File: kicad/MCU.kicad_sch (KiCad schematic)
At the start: 75 parts

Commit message: Fixed symbol missmatches from upgrading to kicad 6
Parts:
- NT? (x4): symbol Device:Net-Tie_2 -> Device:NetTie_2
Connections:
- net +3V3: now also NT?.2, NT?.2, NT?.2, NT?.2
- net VDD1: now also NT?.1
- net VDDA: now also NT?.1
- net VDDSD: now also NT?.1
- net VREFSD: now also NT?.1

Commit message: Fixed broken connections
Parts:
- removed NT? (x4): Net-Tie_2, symbol Device:NetTie_2
- SW1, SW2: renamed from SW?; symbol Device:Rotary_Encoder_Switch -> Device:RotaryEncoder_Switch
- gave numbers to parts that had none: 69
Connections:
- net VDD1 is gone; now on net +3V3: C59.1, C63.1, C69.1, C70.1, C71.1, U8.17 (VDD), U8.48 (VDD)
- net VDDA is gone; now on net +3V3: C56.2, C60.2, C66.2, U8.9 (VDDA)
- net VDDSD is gone; now on net +3V3: C57.2, C61.2, C67.2, U8.24 (VDDSD)
- net VREFSD is gone; now on net +3V3: C58.2, C62.2, C68.2, U8.25 (VREFSD+)
- net GND: now also SW1.C, SW1.S2, SW2.S2
- net GNDREF: now also SW2.C
- net at R78.2: now also SW2.S1
- net at R73.1, R76.1: now also SW2.A
- net at R74.2, R77.1: now also SW2.B
- net at R62.2, R64.1: now also SW1.B
- net at R61.1, R63.1: now also SW1.A
- net at R67.2: now also SW1.S1
- no-connect marks 6 -> 7
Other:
- moved on the sheet: C59, C63, C69, C70, C71

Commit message: Yeeted SMPSs and small changes
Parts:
- removed C70: 100nF, Capacitor_SMD:C_0805_2012Metric_Pad1.15x1.40mm_HandSolder, symbol Device:C_Small
- added NT? (x4): NetTie_2, symbol Device:NetTie_2
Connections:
- net +3V3: now also NT?.2, NT?.2, NT?.2, NT?.2; no longer C56.2, C57.2, C58.2, C59.1, C60.2, C61.2, C62.2, C63.1, C66.2, C67.2, C68.2, C69.1, C71.1, SW3.2, U8.17 (VDD), U8.24 (VDDSD), U8.25 (VREFSD+), U8.48 (VDD), U8.9 (VDDA)
- net SVOUT_RANGE: no longer names the net of U8.20 (PB2)
- new net VDD1: C59.1, C63.1, C69.1, C71.1, NT?.1, SW3.2, U8.17 (VDD), U8.48 (VDD)
- new net VDDA: C56.2, C60.2, C66.2, NT?.1, U8.9 (VDDA)
- new net VDDSD: C57.2, C61.2, C67.2, NT?.1, U8.24 (VDDSD)
- new net VREFSD: C58.2, C62.2, C68.2, NT?.1, U8.25 (VREFSD+)
- no-connect marks 7 -> 8
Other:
- moved on the sheet: C71

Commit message: Added option to power the 1K5 pullup from 3V3 or VBUS
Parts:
- added JP?: Jumper_2_Open, symbol Jumper:Jumper_2_Open
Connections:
- net +3V3: now also JP?.2 (B)
- net at C73.2, R69.2, R70.2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: now also JP?.1 (A)
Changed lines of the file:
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@@
+    (stroke (width 0) (type default) (color 0 0 0 0))
+  )
+  (wire (pts (xy 85.598 99.06) (xy 82.042 99.06))
     (stroke (width 0) (type default) (color 0 0 0 0))
   )
@@
     (stroke (width 0.254) (type default) (color 0 0 0 0))
   )
+  (wire (pts (xy 82.042 99.06) (xy 82.042 101.346))
+    (stroke (width 0) (type default) (color 0 0 0 0))
+  )
   (wire (pts (xy 31.75 188.722) (xy 31.75 189.992))
     (stroke (width 0) (type default) (color 0 0 0 0))
@@
     (stroke (width 0) (type default) (color 0 0 0 0))
   )
+  (wire (pts (xy 102.616 98.044) (xy 102.616 99.06))
+    (stroke (width 0) (type default) (color 0 0 0 0))
+  )
   (polyline (pts (xy 75.565 79.375) (xy 75.565 15.24))
     (stroke (width 0.254) (type default) (color 0 0 0 0))
@@
     (stroke (width 0) (type default) (color 0 0 0 0))
   )
+  (wire (pts (xy 80.01 101.346) (xy 80.01 103.632))
+    (stroke (width 0) (type default) (color 0 0 0 0))
+  )
   (wire (pts (xy 87.63 106.172) (xy 90.17 106.172))
     (stroke (width 0) (type default) (color 0 0 0 0))
@@
   )
   (wire (pts (xy 153.162 184.15) (xy 162.052 184.15))
+    (stroke (width 0) (type default) (color 0 0 0 0))
+  )
+  (wire (pts (xy 82.042 101.346) (xy 80.01 101.346))
+    (stroke (width 0) (type default) (color 0 0 0 0))
+  )
+  (wire (pts (xy 102.616 99.06) (xy 95.758 99.06))
     (stroke (width 0) (type default) (color 0 0 0 0))
   )
@@
     (pin "3")
   )
+  (symbol (lib_id "Jumper:Jumper_2_Open") (at 90.678 99.06 0) (unit 1)
+    (in_bom yes) (on_board yes) (fields_autoplaced)
+    (property "Reference" "JP?" (id 0) (at 90.678 92.71 0))
+    (property "Value" "Jumper_2_Open" (id 1) (at 90.678 95.25 0))
+    (property "Footprint" "" (id 2) (at 90.678 99.06 0)
+      (effects (font (size 1.27 1.27)) hide)
+    )
+    (property "Datasheet" "~" (id 3) (at 90.678 99.06 0)
+      (effects (font (size 1.27 1.27)) hide)
+    )
+    (pin "1")
+    (pin "2")
+  )
   (symbol (lib_id "Device:NetTie_2") (at 61.214 68.834 0) (unit 1)
     (in_bom yes) (on_board yes) (fields_autoplaced)
@@
     (pin "2")
   )
+  (symbol (lib_id "power:+3V3") (at 102.616 98.044 0) (unit 1)
+    (in_bom yes) (on_board yes) (fields_autoplaced)
+    (property "Reference" "#PWR?" (id 0) (at 102.616 101.854 0)
+      (effects (font (size 1.27 1.27)) hide)
+    )
+    (property "Value" "+3V3" (id 1) (at 102.616 92.964 0))
+    (property "Footprint" "" (id 2) (at 102.616 98.044 0)
+      (effects (font (size 1.27 1.27)) hide)
+    )
+    (property "Datasheet" "" (id 3) (at 102.616 98.044 0)
+      (effects (font (size 1.27 1.27)) hide)
+    )
+    (pin "1")
+  )
   (symbol (lib_id "Device:NetTie_2") (at 51.816 37.592 0) (unit 1)

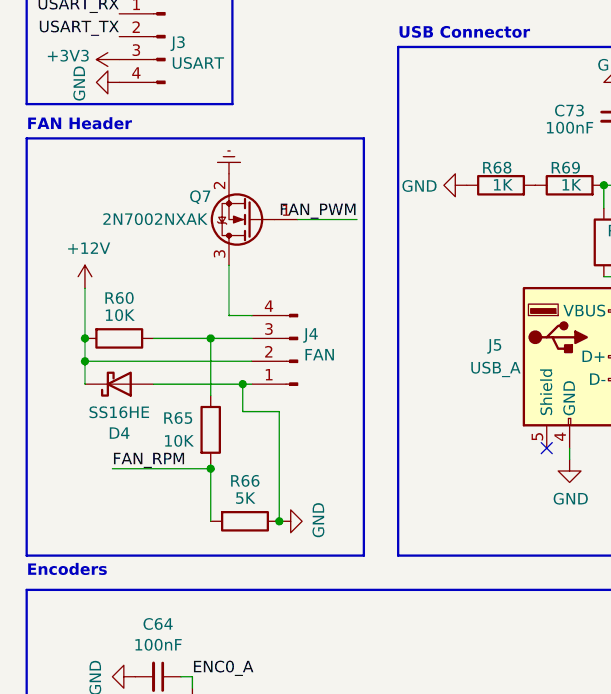
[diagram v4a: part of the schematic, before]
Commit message: Fixed fan rpm reading circuitry
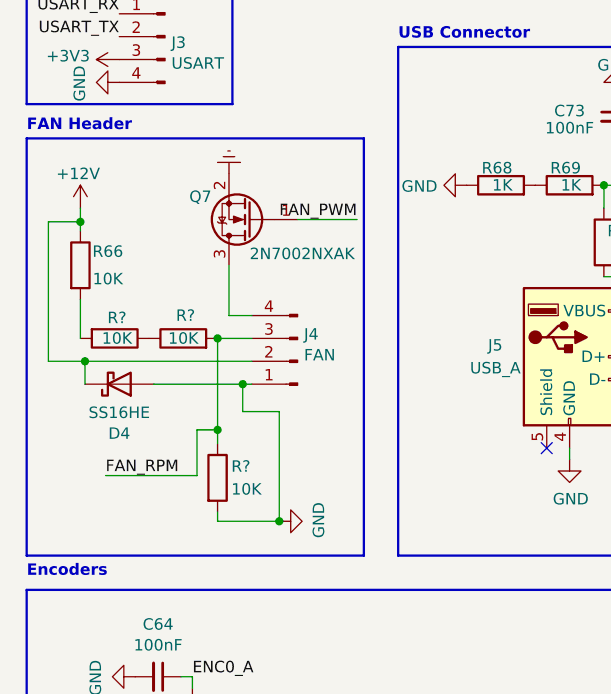
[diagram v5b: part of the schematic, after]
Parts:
- removed R60, R65: 10K, symbol Device:R
- added R? (x3): 10K, symbol Device:R
- R66: value 5K -> 10K
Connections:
- net +12V: now also R66.1
- net FAN_RPM: now also J4.3 (Pin_3), R?.1, R?.2; no longer R66.2
- net GND: now also R?.2; no longer R66.1
- new net: R66.2, R?.2
- new net: R?.1, R?.1
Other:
- moved on the sheet: R66

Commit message: Changes
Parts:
- removed R82: 1K, Resistor_SMD:R_0805_2012Metric_Pad1.15x1.40mm_HandSolder, symbol Device:R
- added R? (x2): 100R, symbol Device:R
- J4: footprint (none) -> Connector:FanPinHeader_1x04_P2.54mm_Vertical
- R81: value 1K -> 4K7
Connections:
- net FAN_PWM: now also R?.2; no longer Q7.1 (G)
- net FAN_RPM: now also R?.1; no longer J4.3 (Pin_3), R?.1, R?.2
- new net: J4.3 (Pin_3), R?.1, R?.2, R?.2
- new net: Q7.1 (G), R?.1
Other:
- moved on the sheet: Q7
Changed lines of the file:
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@@
   (junction (at 36.83 73.914) (diameter 0) (color 0 0 0 0)
   )
-  (junction (at 145.542 184.15) (diameter 0) (color 0 0 0 0)
-  )
   (junction (at 80.01 106.172) (diameter 0) (color 0 0 0 0)
   )
@@
   )
   (junction (at 36.83 54.102) (diameter 0) (color 0 0 0 0)
-  )
-  (junction (at 153.162 184.15) (diameter 0) (color 0 0 0 0)
   )
   (junction (at 31.75 173.482) (diameter 0) (color 0 0 0 0)
@@
     (stroke (width 0) (type default) (color 0 0 0 0))
   )
-  (wire (pts (xy 43.434 109.982) (xy 50.038 109.982))
-    (stroke (width 0) (type default) (color 0 0 0 0))
-  )
   (wire (pts (xy 29.21 178.562) (xy 31.75 178.562))
     (stroke (width 0) (type default) (color 0 0 0 0))
@@
     (stroke (width 0) (type default) (color 0 0 0 0))
   )
+  (wire (pts (xy 35.814 118.364) (xy 35.814 120.65))
+    (stroke (width 0) (type default) (color 0 0 0 0))
+  )
   (polyline (pts (xy 121.92 147.32) (xy 121.92 90.805))
     (stroke (width 0.254) (type default) (color 0 0 0 0))
@@
     (stroke (width 0) (type default) (color 0 0 0 0))
   )
+  (wire (pts (xy 35.814 120.65) (xy 38.354 120.65))
+    (stroke (width 0) (type default) (color 0 0 0 0))
+  )
   (wire (pts (xy 150.622 40.132) (xy 148.844 40.132))
     (stroke (width 0) (type default) (color 0 0 0 0))
@@
     (stroke (width 0) (type default) (color 0 0 0 0))
   )
-  (wire (pts (xy 35.814 115.062) (xy 35.814 120.65))
-    (stroke (width 0) (type default) (color 0 0 0 0))
-  )
   (wire (pts (xy 145.542 124.46) (xy 145.542 126.492))
     (stroke (width 0) (type default) (color 0 0 0 0))
@@
     (stroke (width 0) (type default) (color 0 0 0 0))
   )
-  (wire (pts (xy 153.162 184.15) (xy 153.162 187.96))
-    (stroke (width 0) (type default) (color 0 0 0 0))
-  )
   (polyline (pts (xy 130.81 151.13) (xy 13.335 151.13))
     (stroke (width 0.254) (type default) (color 0 0 0 0))
@@
     (stroke (width 0) (type default) (color 0 0 0 0))
   )
-  (wire (pts (xy 22.098 138.43) (xy 32.258 138.43))
+  (wire (pts (xy 16.002 138.43) (xy 24.638 138.43))
     (stroke (width 0) (type default) (color 0 0 0 0))
   )
@@
     (stroke (width 0) (type default) (color 0 0 0 0))
   )
+  (wire (pts (xy 42.672 109.982) (xy 50.292 109.982))
+    (stroke (width 0) (type default) (color 0 0 0 0))
+  )
   (wire (pts (xy 120.65 45.212) (xy 150.622 45.212))
     (stroke (width 0) (type default) (color 0 0 0 0))
@@
     (stroke (width 0) (type default) (color 0 0 0 0))
   )
+  (wire (pts (xy 27.432 115.062) (xy 27.432 118.364))
+    (stroke (width 0) (type default) (color 0 0 0 0))
+  )
   (wire (pts (xy 36.83 68.834) (xy 48.26 68.834))
     (stroke (width 0) (type default) (color 0 0 0 0))
   )
-  (wire (pts (xy 35.814 120.65) (xy 38.354 120.65))
-    (stroke (width 0) (type default) (color 0 0 0 0))
-  )
   (wire (pts (xy 96.52 113.792) (xy 96.52 116.332))
     (stroke (width 0) (type default) (color 0 0 0 0))
@@
     (stroke (width 0) (type default) (color 0 0 0 0))
   )
+  (wire (pts (xy 27.432 118.364) (xy 35.814 118.364))
+    (stroke (width 0) (type default) (color 0 0 0 0))
+  )
   (polyline (pts (xy 165.735 147.32) (xy 165.735 120.65))
     (stroke (width 0.254) (type default) (color 0 0 0 0))
-  )
-  (wire (pts (xy 145.542 184.15) (xy 145.542 187.96))
-    (stroke (width 0) (type default) (color 0 0 0 0))
   )
   (wire (pts (xy 160.782 186.69) (xy 160.782 188.722))
@@
     (effects (font (size 1.27 1.27)) (justify right bottom))
   )
-  (label "FAN_RPM" (at 22.098 138.43 0)
+  (label "FAN_RPM" (at 16.002 138.43 0)
     (effects (font (size 1.27 1.27)) (justify left bottom))
   )
@@
     (effects (font (size 1.27 1.27)) (justify right bottom))
   )
-  (label "FAN_PWM" (at 50.038 109.982 180)
+  (label "FAN_PWM" (at 50.292 109.982 180)
     (effects (font (size 1.27 1.27)) (justify right bottom))
   )
@@
     (pin "1")
   )
-  (symbol (lib_id "Device:R") (at 149.352 187.96 90) (unit 1)
-    (in_bom yes) (on_board yes)
-    (property "Reference" "R82" (id 0) (at 143.002 186.69 90))
-    (property "Value" "1K" (id 1) (at 154.432 186.69 90))
-    (property "Footprint" "Resistor_SMD:R_0805_2012Metric_Pad1.15x1.40mm_HandSolder" (id 2) (at 149.352 189.738 90)
-      (effects (font (size 1.27 1.27)) hide)
-    )
-    (property "Datasheet" "https://www.mouser.se/datasheet/2/447/PYu-RT_1-to-0.01_RoHS_L_9-1222720.pdf" (id 3) (at 149.352 187.96 0)
-      (effects (font (size 1.27 1.27)) hide)
-    )
-    (property "MPN" "RT0805FRE071KL" (id 4) (at 149.352 187.96 0)
-      (effects (font (size 1.27 1.27)) hide)
-    )
-    (pin "1")
-    (pin "2")
-  )
   (symbol (lib_id "power:+3V3") (at 140.462 184.15 90) (unit 1)
     (in_bom yes) (on_board yes)
@@
   (symbol (lib_id "Device:R") (at 149.352 184.15 90) (unit 1)
     (in_bom yes) (on_board yes)
-    (property "Reference" "R81" (id 0) (at 143.002 182.88 90))
-    (property "Value" "1K" (id 1) (at 154.432 182.88 90))
+    (property "Reference" "R81" (id 0) (at 149.352 186.436 90))
+    (property "Value" "4K7" (id 1) (at 149.352 184.15 90))
     (property "Footprint" "Resistor_SMD:R_0805_2012Metric_Pad1.15x1.40mm_HandSolder" (id 2) (at 149.352 185.928 90)
       (effects (font (size 1.27 1.27)) hide)
@@
       (effects (font (size 1.27 1.27)) (justify right))
     )
-    (property "Footprint" "" (id 2) (at 43.434 125.73 0)
+    (property "Footprint" "Connector:FanPinHeader_1x04_P2.54mm_Vertical" (id 2) (at 43.434 125.73 0)
       (effects (font (size 1.27 1.27)) hide)
     )
@@
     (pin "2")
   )
-  (symbol (lib_id "Device:Q_NMOS_GSD") (at 38.354 109.982 180) (unit 1)
-    (in_bom yes) (on_board yes)
-    (property "Reference" "Q7" (id 0) (at 32.639 107.442 0))
-    (property "Value" "2N7002NXAK" (id 1) (at 43.942 113.792 0))
-    (property "Footprint" "Package_TO_SOT_SMD:SOT-23" (id 2) (at 33.274 112.522 0)
-      (effects (font (size 1.27 1.27)) hide)
-    )
-    (property "Datasheet" "https://assets.nexperia.com/documents/data-sheet/2N7002NXAK.pdf" (id 3) (at 38.354 109.982 0)
-      (effects (font (size 1.27 1.27)) hide)
-    )
-    (property "MPN" "2N7002NXAK" (id 4) (at 38.354 109.982 90)
+  (symbol (lib_id "Device:Q_NMOS_GSD") (at 29.972 109.982 180) (unit 1)
+    (in_bom yes) (on_board yes)
+    (property "Reference" "Q7" (id 0) (at 24.257 107.442 0))
+    (property "Value" "2N7002NXAK" (id 1) (at 35.56 113.792 0))
+    (property "Footprint" "Package_TO_SOT_SMD:SOT-23" (id 2) (at 24.892 112.522 0)
+      (effects (font (size 1.27 1.27)) hide)
+    )
+    (property "Datasheet" "https://assets.nexperia.com/documents/data-sheet/2N7002NXAK.pdf" (id 3) (at 29.972 109.982 0)
+      (effects (font (size 1.27 1.27)) hide)
+    )
+    (property "MPN" "2N7002NXAK" (id 4) (at 29.972 109.982 90)
       (effects (font (size 1.27 1.27)) hide)
     )
@@
     (pin "3")
   )
-  (symbol (lib_id "power:GNDREF") (at 35.814 104.902 180) (unit 1)
-    (in_bom yes) (on_board yes)
-    (property "Reference" "#PWR062" (id 0) (at 35.814 98.552 0)
-      (effects (font (size 1.27 1.27)) hide)
-    )
-    (property "Value" "GNDREF" (id 1) (at 35.687 100.5078 0)
-      (effects (font (size 1.27 1.27)) hide)
-    )
-    (property "Footprint" "" (id 2) (at 35.814 104.902 0)
-      (effects (font (size 1.27 1.27)) hide)
-    )
-    (property "Datasheet" "" (id 3) (at 35.814 104.902 0)
+  (symbol (lib_id "power:GNDREF") (at 27.432 104.902 180) (unit 1)
+    (in_bom yes) (on_board yes)
+    (property "Reference" "#PWR062" (id 0) (at 27.432 98.552 0)
+      (effects (font (size 1.27 1.27)) hide)
+    )
+    (property "Value" "GNDREF" (id 1) (at 27.305 100.5078 0)
+      (effects (font (size 1.27 1.27)) hide)
+    )
+    (property "Footprint" "" (id 2) (at 27.432 104.902 0)
+      (effects (font (size 1.27 1.27)) hide)
+    )
+    (property "Datasheet" "" (id 3) (at 27.432 104.902 0)
       (effects (font (size 1.27 1.27)) hide)
     )
@@
     (pin "1")
   )
+  (symbol (lib_id "Device:R") (at 28.448 138.43 90) (unit 1)
+    (in_bom yes) (on_board yes)
+    (property "Reference" "R?" (id 0) (at 28.448 135.89 90))
+    (property "Value" "100R" (id 1) (at 28.448 138.43 90))
+    (property "Footprint" "" (id 2) (at 28.448 140.208 90)
+      (effects (font (size 1.27 1.27)) hide)
+    )
+    (property "Datasheet" "~" (id 3) (at 28.448 138.43 0)
+      (effects (font (size 1.27 1.27)) hide)
+    )
+    (pin "1")
+    (pin "2")
+  )
+  (symbol (lib_id "Device:R") (at 38.862 109.982 90) (unit 1)
+    (in_bom yes) (on_board yes)
+    (property "Reference" "R?" (id 0) (at 38.862 107.442 90))
+    (property "Value" "100R" (id 1) (at 38.862 109.982 90))
+    (property "Footprint" "" (id 2) (at 38.862 111.76 90)
+      (effects (font (size 1.27 1.27)) hide)
+    )
+    (property "Datasheet" "~" (id 3) (at 38.862 109.982 0)
+      (effects (font (size 1.27 1.27)) hide)
+    )
+    (pin "1")
+    (pin "2")
+  )
   (symbol (lib_id "Device:NetTie_2") (at 51.816 37.592 0) (unit 1)
